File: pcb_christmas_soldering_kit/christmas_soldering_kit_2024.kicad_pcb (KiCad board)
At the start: 2 copper layers, 79.8 x 99.3 mm, 26 parts, among them J3 Conn_Out, J4 Conn_In, J5 J_In, P1 Conn_01x08_Pin, P2 Conn_01x08_Pin, SW1 Button, U1 ESP32-C3, U2 TC4427CPA

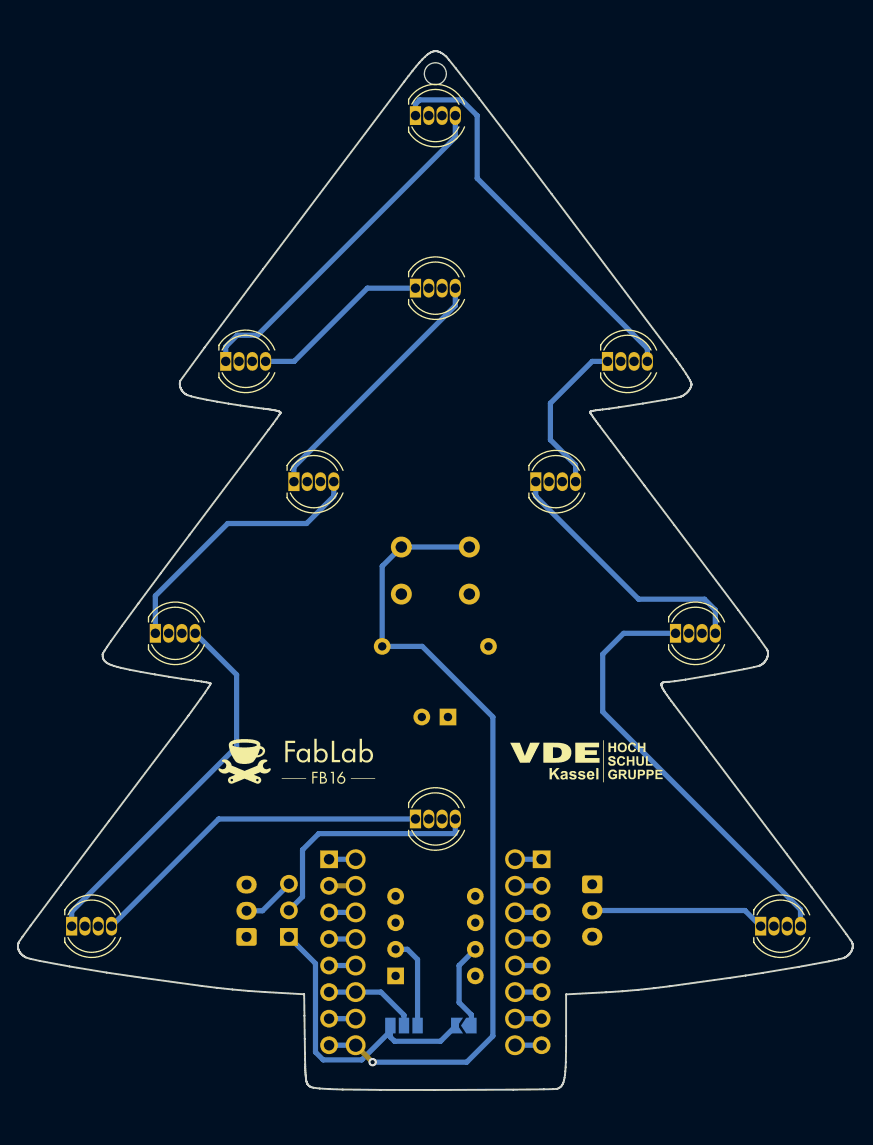
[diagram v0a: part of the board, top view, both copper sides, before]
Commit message: prototype 2: remove unnecessary components, improve LED footprints
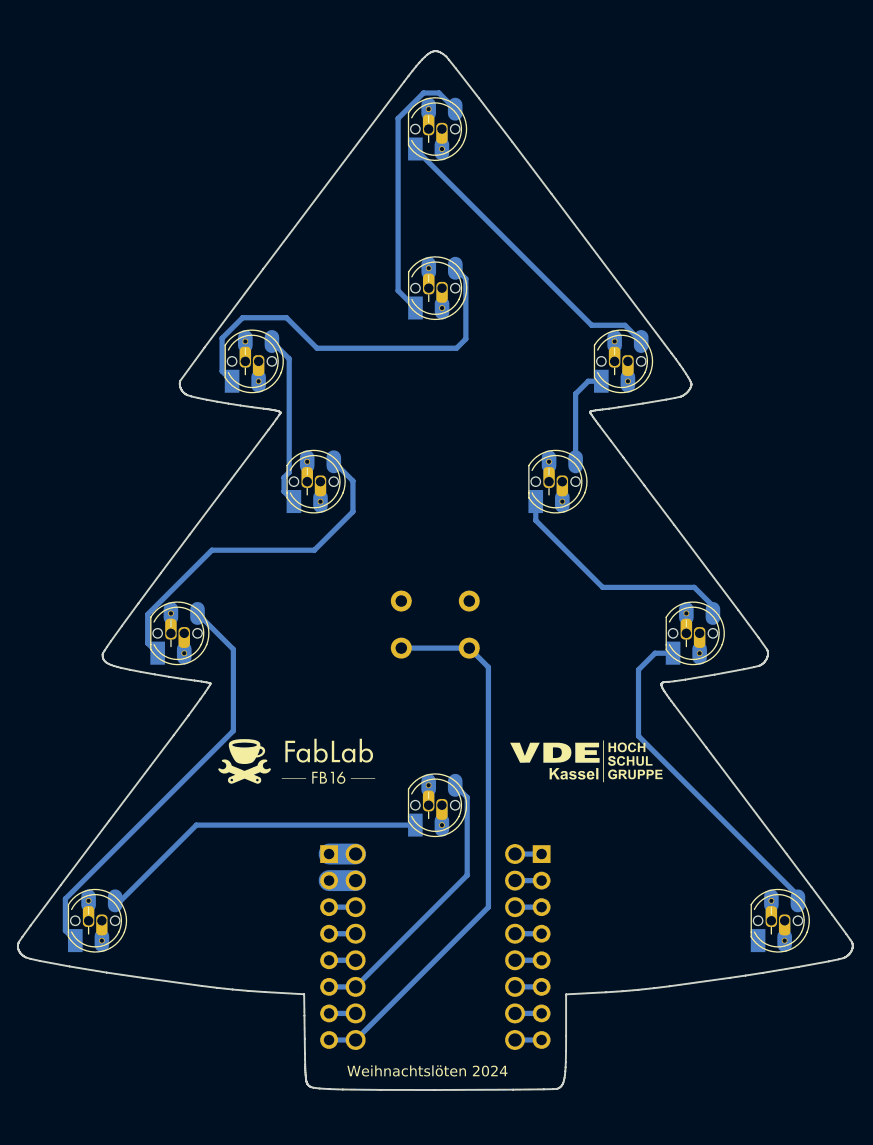
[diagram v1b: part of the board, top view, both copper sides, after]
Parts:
- removed C1: 470uF, Capacitor_THT:CP_Radial_D5.0mm_P2.50mm
- removed J3: Conn_Out, Connector_JST:JST_XH_S3B-XH-A_1x03_P2.50mm_Horizontal
- removed J4: Conn_In, Connector_JST:JST_XH_S3B-XH-A_1x03_P2.50mm_Horizontal
- removed J5: J_In, Connector_PinHeader_2.54mm:PinHeader_1x03_P2.54mm_Vertical
- removed JP1: J_LED_DATA_3.3V, Jumper:SolderJumper-3_P1.3mm_Open_Pad1.0x1.5mm_NumberLabels
- removed JP2: J_LED_DATA_5V, Jumper:SolderJumper-2_P1.3mm_Open_TrianglePad1.0x1.5mm
- removed R1: 10k, Resistor_THT:R_Axial_DIN0207_L6.3mm_D2.5mm_P10.16mm_Horizontal
- removed REF**: MountingHole_2.1mm, MountingHole:MountingHole_2.1mm
- removed U2: TC4427CPA, Package_DIP:DIP-8_W7.62mm
- D1, D10, D11, D2, D3, D4, D5, D6, D7, D8, D9: footprint LED_THT:LED_D5.0mm-4_RGB -> Library:LED_D5.0mm-4_RGB_easy
- moved D6 19.4 mm to (148.6, 65.5)
- moved D5 18.9 mm to (131.1, 72.5)
- moved SW1 11.6 mm to (147.2, 99.9), turned to 0 degrees
- moved D1 1.32 mm to (148.6, 114.9)
- moved D7 1.29 mm to (148.6, 50.3)
- moved D2 0.63 mm to (116.1, 126.0)
- moved D8 0.59 mm to (166.4, 72.5)
- moved D11 0.58 mm to (181.4, 126.0)
- moved P1 0.50 mm to (140.3, 119.6)
- moved P2 0.50 mm to (160.7, 119.6)
- moved U1 0.50 mm to (150.5, 129.5)
- moved D10 0.23 mm to (173.2, 98.5)
- moved D3 0.22 mm to (124.0, 98.5)
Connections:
- D1 pad 4: Net-(D1-DI) -> GPIO2
- D11 pad 1: Net-(D11-DO) -> unconnected-(D11-DO-Pad1)
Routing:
- net LED_DATA: track 28.9 -> 0.00 mm
- net GPIO0: track 78.0 -> 53.0 mm, vias 1 -> 0
- net Net-(D1-DI): track 23.0 -> 0.00 mm
- net Net-(D5-DO): track 17.2 -> 37.4 mm
- net GPIO2: track 9.32 -> 26.7 mm
- net Net-(D11-DO): track 16.7 -> 0.00 mm
- net Net-(D10-DO): track 41.6 -> 32.4 mm
- net Net-(JP1-B): track 9.07 -> 0.00 mm
- net Net-(D7-DO): track 38.0 -> 29.2 mm
- net Net-(JP2-A): track 8.42 -> 0.00 mm
- net Net-(D4-DO): track 24.9 -> 16.6 mm
- net Net-(D6-DO): track 33.7 -> 25.9 mm
- net Net-(D3-DO): track 26.0 -> 33.3 mm
- net Net-(D8-DO): track 15.6 -> 9.45 mm
- net Net-(J4-Pin_2): track 5.15 -> 0.00 mm
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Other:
- board text added: "Prototyp 2"
- board text added: "Weihnachtslöten 2024"
